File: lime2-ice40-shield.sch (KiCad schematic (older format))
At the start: 5 parts

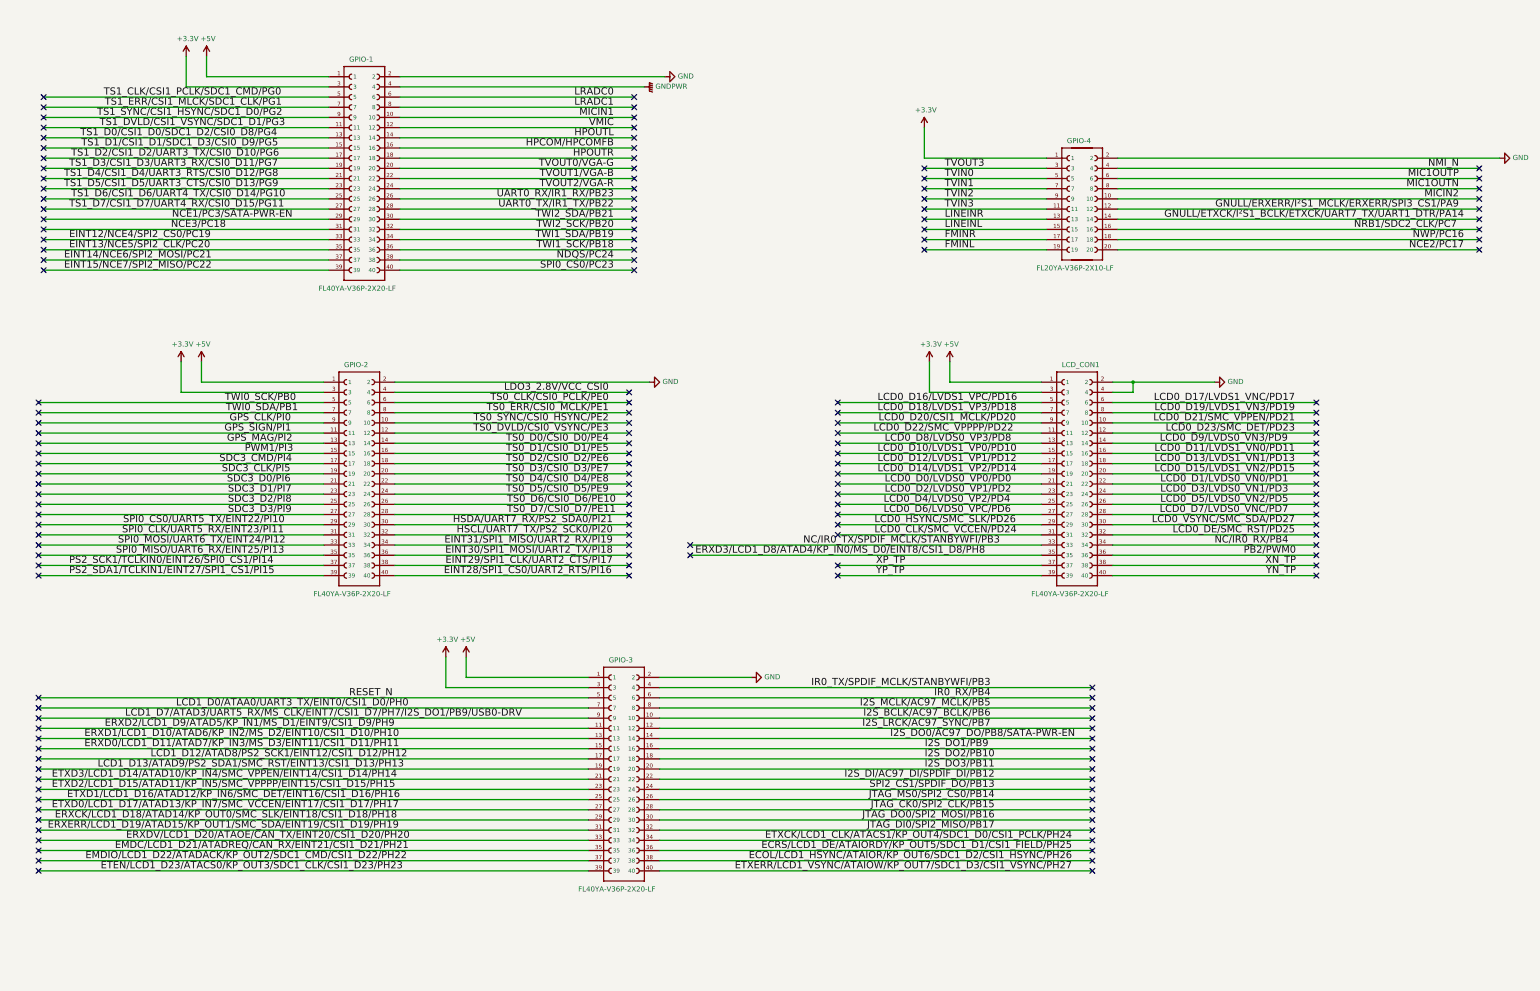
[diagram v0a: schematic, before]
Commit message: Clean up lime2 header connections
Left only those that will be used

Signed-off-by: Rangel Ivanov <rangelivanov88@gmail.com>
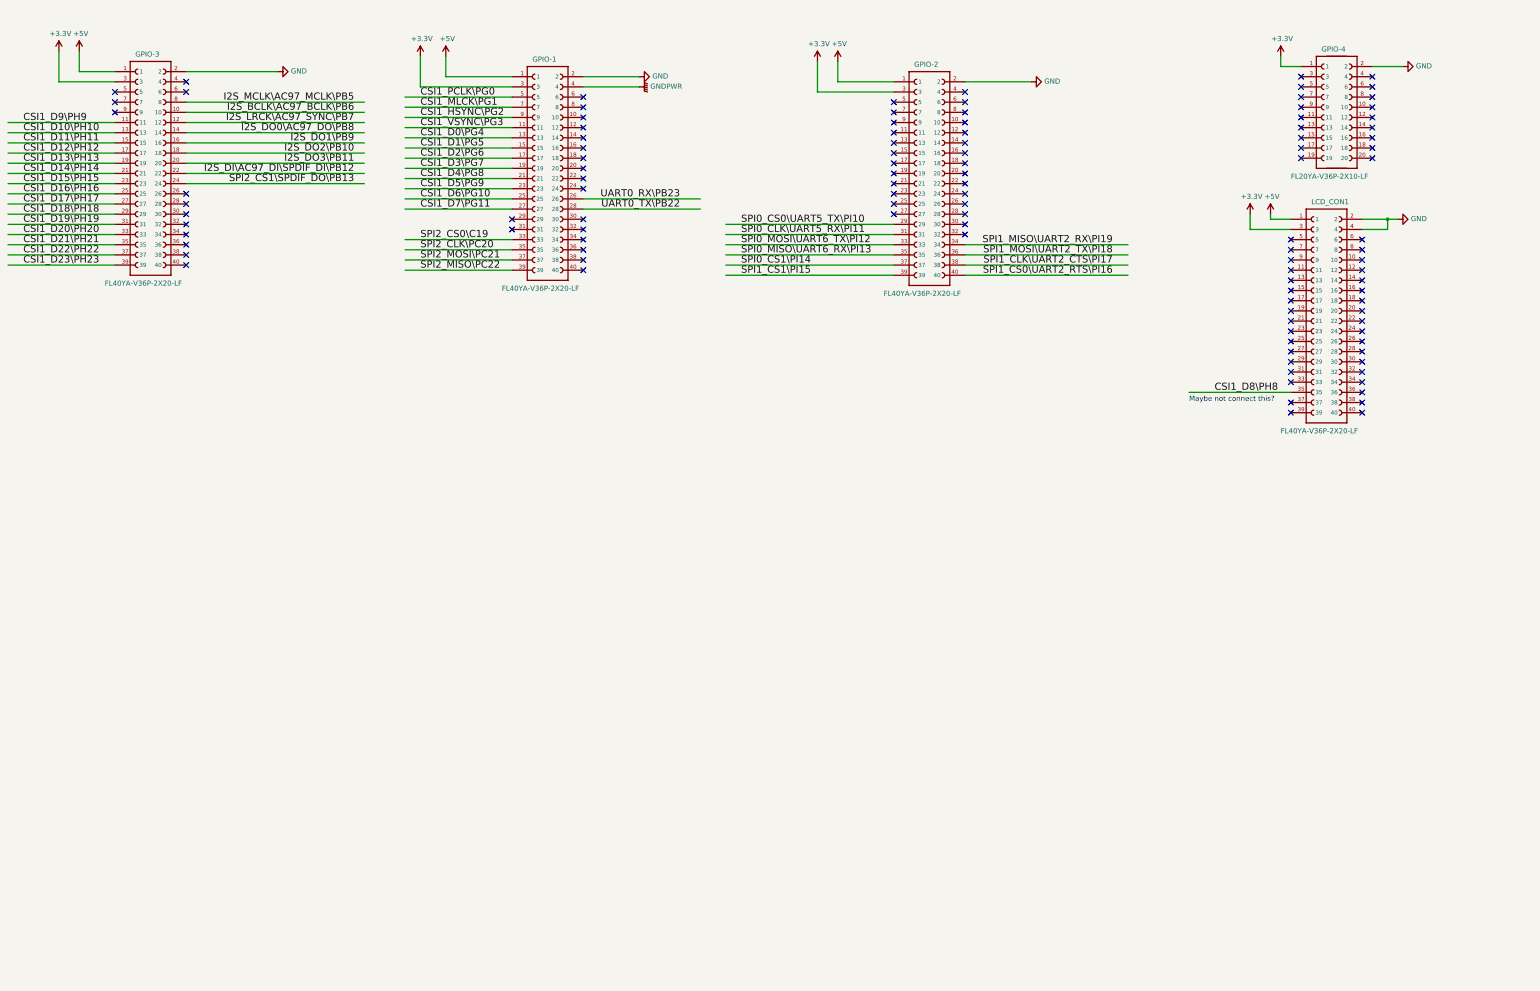
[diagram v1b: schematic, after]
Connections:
- net labels added: CSI1_D0\PG4, CSI1_D10\PH10, CSI1_D11\PH11, CSI1_D12\PH12, CSI1_D13\PH13, CSI1_D14\PH14, CSI1_D15\PH15, CSI1_D16\PH16, CSI1_D17\PH17, CSI1_D18\PH18, CSI1_D19\PH19, CSI1_D1\PG5, CSI1_D20\PH20, CSI1_D21\PH21, CSI1_D22\PH22, CSI1_D23\PH23, CSI1_D2\PG6, CSI1_D3\PG7, CSI1_D4\PG8, CSI1_D5\PG9, CSI1_D6\PG10, CSI1_D7\PG11, CSI1_D8\PH8, CSI1_D9\PH9, CSI1_HSYNC\PG2, CSI1_MLCK\PG1, CSI1_PCLK\PG0, CSI1_VSYNC\PG3, I2S_BCLK\AC97_BCLK\PB6, I2S_DI\AC97_DI\SPDIF_DI\PB12, I2S_DO0\AC97_DO\PB8, I2S_DO1\PB9, I2S_DO2\PB10, I2S_DO3\PB11, I2S_LRCK\AC97_SYNC\PB7, I2S_MCLK\AC97_MCLK\PB5, SPI0_CLK\UART5_RX\PI11, SPI0_CS0\UART5_TX\PI10, SPI0_CS1\PI14, SPI0_MISO\UART6_RX\PI13, SPI0_MOSI\UART6_TX\PI12, SPI1_CLK\UART2_CTS\PI17, SPI1_CS0\UART2_RTS\PI16, SPI1_CS1\PI15, SPI1_MISO\UART2_RX\PI19, SPI1_MOSI\UART2_TX\PI18, SPI2_CLK\PC20, SPI2_CS0\C19, SPI2_CS1\SPDIF_DO\PB13, SPI2_MISO\PC22, SPI2_MOSI\PC21, UART0_RX\PB23, UART0_TX\PB22
- net labels removed: ECOL/LCD1_HSYNC/ATAIOR/KP_OUT6/SDC1_D2/CSI1_HSYNC/PH26, ECRS/LCD1_DE/ATAIORDY/KP_OUT5/SDC1_D1/CSI1_FIELD/PH25, EINT12/NCE4/SPI2_CS0/PC19, EINT13/NCE5/SPI2_CLK/PC20, EINT14/NCE6/SPI2_MOSI/PC21, EINT15/NCE7/SPI2_MISO/PC22, EINT28/SPI1_CS0/UART2_RTS/PI16, EINT29/SPI1_CLK/UART2_CTS/PI17, EINT30/SPI1_MOSI/UART2_TX/PI18, EINT31/SPI1_MISO/UART2_RX/PI19, EMDC/LCD1_D21/ATADREQ/CAN_RX/EINT21/CSI1_D21/PH21, EMDIO/LCD1_D22/ATADACK/KP_OUT2/SDC1_CMD/CSI1_D22/PH22, ERXCK/LCD1_D18/ATAD14/KP_OUT0/SMC_SLK/EINT18/CSI1_D18/PH18, ERXD0/LCD1_D11/ATAD7/KP_IN3/MS_D3/EINT11/CSI1_D11/PH11, ERXD1/LCD1_D10/ATAD6/KP_IN2/MS_D2/EINT10/CSI1_D10/PH10, ERXD2/LCD1_D9/ATAD5/KP_IN1/MS_D1/EINT9/CSI1_D9/PH9, ERXD3/LCD1_D8/ATAD4/KP_IN0/MS_D0/EINT8/CSI1_D8/PH8, ERXDV/LCD1_D20/ATAOE/CAN_TX/EINT20/CSI1_D20/PH20, ERXERR/LCD1_D19/ATAD15/KP_OUT1/SMC_SDA/EINT19/CSI1_D19/PH19, ETEN/LCD1_D23/ATACS0/KP_OUT3/SDC1_CLK/CSI1_D23/PH23, ETXCK/LCD1_CLK/ATACS1/KP_OUT4/SDC1_D0/CSI1_PCLK/PH24, ETXD0/LCD1_D17/ATAD13/KP_IN7/SMC_VCCEN/EINT17/CSI1_D17/PH17, ETXD1/LCD1_D16/ATAD12/KP_IN6/SMC_DET/EINT16/CSI1_D16/PH16, ETXD2/LCD1_D15/ATAD11/KP_IN5/SMC_VPPPP/EINT15/CSI1_D15/PH15, ETXD3/LCD1_D14/ATAD10/KP_IN4/SMC_VPPEN/EINT14/CSI1_D14/PH14, ETXERR/LCD1_VSYNC/ATAIOW/KP_OUT7/SDC1_D3/CSI1_VSYNC/PH27, FMINL, FMINR, GNULL/ERXERR/I²S1_MCLK/ERXERR/SPI3_CS1/PA9, GNULL/ETXCK/I²S1_BCLK/ETXCK/UART7_TX/UART1_DTR/PA14, GPS_CLK/PI0, GPS_MAG/PI2, GPS_SIGN/PI1, HPCOM/HPCOMFB, HPOUTL, HPOUTR, HSCL/UART7_TX/PS2_SCK0/PI20, HSDA/UART7_RX/PS2_SDA0/PI21, I2S_BCLK/AC97_BCLK/PB6, I2S_DI/AC97_DI/SPDIF_DI/PB12, I2S_DO0/AC97_DO/PB8/SATA-PWR-EN, I2S_DO1/PB9, I2S_DO2/PB10, I2S_DO3/PB11, I2S_LRCK/AC97_SYNC/PB7, I2S_MCLK/AC97_MCLK/PB5, IR0_RX/PB4, IR0_TX/SPDIF_MCLK/STANBYWFI/PB3, JTAG_CK0/SPI2_CLK/PB15, JTAG_DI0/SPI2_MISO/PB17, JTAG_DO0/SPI2_MOSI/PB16, JTAG_MS0/SPI2_CS0/PB14, LCD0_CLK/SMC_VCCEN/PD24, LCD0_D0/LVDS0_VP0/PD0, LCD0_D1/LVDS0_VN0/PD1, LCD0_D10/LVDS1_VP0/PD10, LCD0_D11/LVDS1_VN0/PD11, LCD0_D12/LVDS1_VP1/PD12, LCD0_D13/LVDS1_VN1/PD13, LCD0_D14/LVDS1_VP2/PD14, LCD0_D15/LVDS1_VN2/PD15, LCD0_D16/LVDS1_VPC/PD16, LCD0_D17/LVDS1_VNC/PD17, LCD0_D18/LVDS1_VP3/PD18, LCD0_D19/LVDS1_VN3/PD19, LCD0_D2/LVDS0_VP1/PD2, LCD0_D20/CSI1_MCLK/PD20, LCD0_D21/SMC_VPPEN/PD21, LCD0_D22/SMC_VPPPP/PD22, LCD0_D23/SMC_DET/PD23, LCD0_D3/LVDS0_VN1/PD3, LCD0_D4/LVDS0_VP2/PD4, LCD0_D5/LVDS0_VN2/PD5, LCD0_D6/LVDS0_VPC/PD6, LCD0_D7/LVDS0_VNC/PD7, LCD0_D8/LVDS0_VP3/PD8, LCD0_D9/LVDS0_VN3/PD9, LCD0_DE/SMC_RST/PD25, LCD0_HSYNC/SMC_SLK/PD26, LCD0_VSYNC/SMC_SDA/PD27, LCD1_D0/ATAA0/UART3_TX/EINT0/CSI1_D0/PH0, LCD1_D12/ATAD8/PS2_SCK1/EINT12/CSI1_D12/PH12, LCD1_D13/ATAD9/PS2_SDA1/SMC_RST/EINT13/CSI1_D13/PH13, LCD1_D7/ATAD3/UART5_RX/MS_CLK/EINT7/CSI1_D7/PH7/I2S_DO1/PB9/USB0-DRV, LDO3_2.8V/VCC_CSI0, LINEINL, LINEINR, LRADC0, LRADC1, MIC1OUTN, MIC1OUTP, MICIN1, MICIN2, NC/IR0_RX/PB4, NC/IR0_TX/SPDIF_MCLK/STANBYWFI/PB3, NCE1/PC3/SATA-PWR-EN, NCE2/PC17, NCE3/PC18, NDQS/PC24, NMI_N, NRB1/SDC2_CLK/PC7, NWP/PC16, PB2/PWM0, PS2_SCK1/TCLKIN0/EINT26/SPI0_CS1/PI14, PS2_SDA1/TCLKIN1/EINT27/SPI1_CS1/PI15, PWM1/PI3, RESET_N, SDC3_CLK/PI5, SDC3_CMD/PI4, SDC3_D0/PI6, SDC3_D1/PI7, SDC3_D2/PI8, SDC3_D3/PI9, SPI0_CLK/UART5_RX/EINT23/PI11, SPI0_CS0/PC23, SPI0_CS0/UART5_TX/EINT22/PI10, SPI0_MISO/UART6_RX/EINT25/PI13, SPI0_MOSI/UART6_TX/EINT24/PI12, SPI2_CS1/SPDIF_DO/PB13, TS0_CLK/CSI0_PCLK/PE0, TS0_D0/CSI0_D0/PE4, TS0_D1/CSI0_D1/PE5, TS0_D2/CSI0_D2/PE6, TS0_D3/CSI0_D3/PE7, TS0_D4/CSI0_D4/PE8, TS0_D5/CSI0_D5/PE9, TS0_D6/CSI0_D6/PE10, TS0_D7/CSI0_D7/PE11, TS0_DVLD/CSI0_VSYNC/PE3, TS0_ERR/CSI0_MCLK/PE1, TS0_SYNC/CSI0_HSYNC/PE2, TS1_CLK/CSI1_PCLK/SDC1_CMD/PG0, TS1_D0/CSI1_D0/SDC1_D2/CSI0_D8/PG4, TS1_D1/CSI1_D1/SDC1_D3/CSI0_D9/PG5, TS1_D2/CSI1_D2/UART3_TX/CSI0_D10/PG6, TS1_D3/CSI1_D3/UART3_RX/CSI0_D11/PG7, TS1_D4/CSI1_D4/UART3_RTS/CSI0_D12/PG8, TS1_D5/CSI1_D5/UART3_CTS/CSI0_D13/PG9, TS1_D6/CSI1_D6/UART4_TX/CSI0_D14/PG10, TS1_D7/CSI1_D7/UART4_RX/CSI0_D15/PG11, TS1_DVLD/CSI1_VSYNC/SDC1_D1/PG3, TS1_ERR/CSI1_MLCK/SDC1_CLK/PG1, TS1_SYNC/CSI1_HSYNC/SDC1_D0/PG2, TVIN0, TVIN1, TVIN2, TVIN3, TVOUT0/VGA-G, TVOUT1/VGA-B, TVOUT2/VGA-R, TVOUT3, TWI0_SCK/PB0, TWI0_SDA/PB1, TWI1_SCK/PB18, TWI1_SDA/PB19, TWI2_SCK/PB20, TWI2_SDA/PB21, UART0_RX/IR1_RX/PB23, UART0_TX/IR1_TX/PB22, VMIC, XN_TP, XP_TP, YN_TP, YP_TP
- wire segments 191 -> 80
- no-connect marks 164 -> 111
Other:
- note added: "Maybe not connect this?\n"
- moved on the sheet: GPIO-1, GPIO-2, GPIO-3, GPIO-4, LCD_CON1

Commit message: Initial routing of CSI1 signals
Signed-off-by: Rangel Ivanov <rangelivanov88@gmail.com>
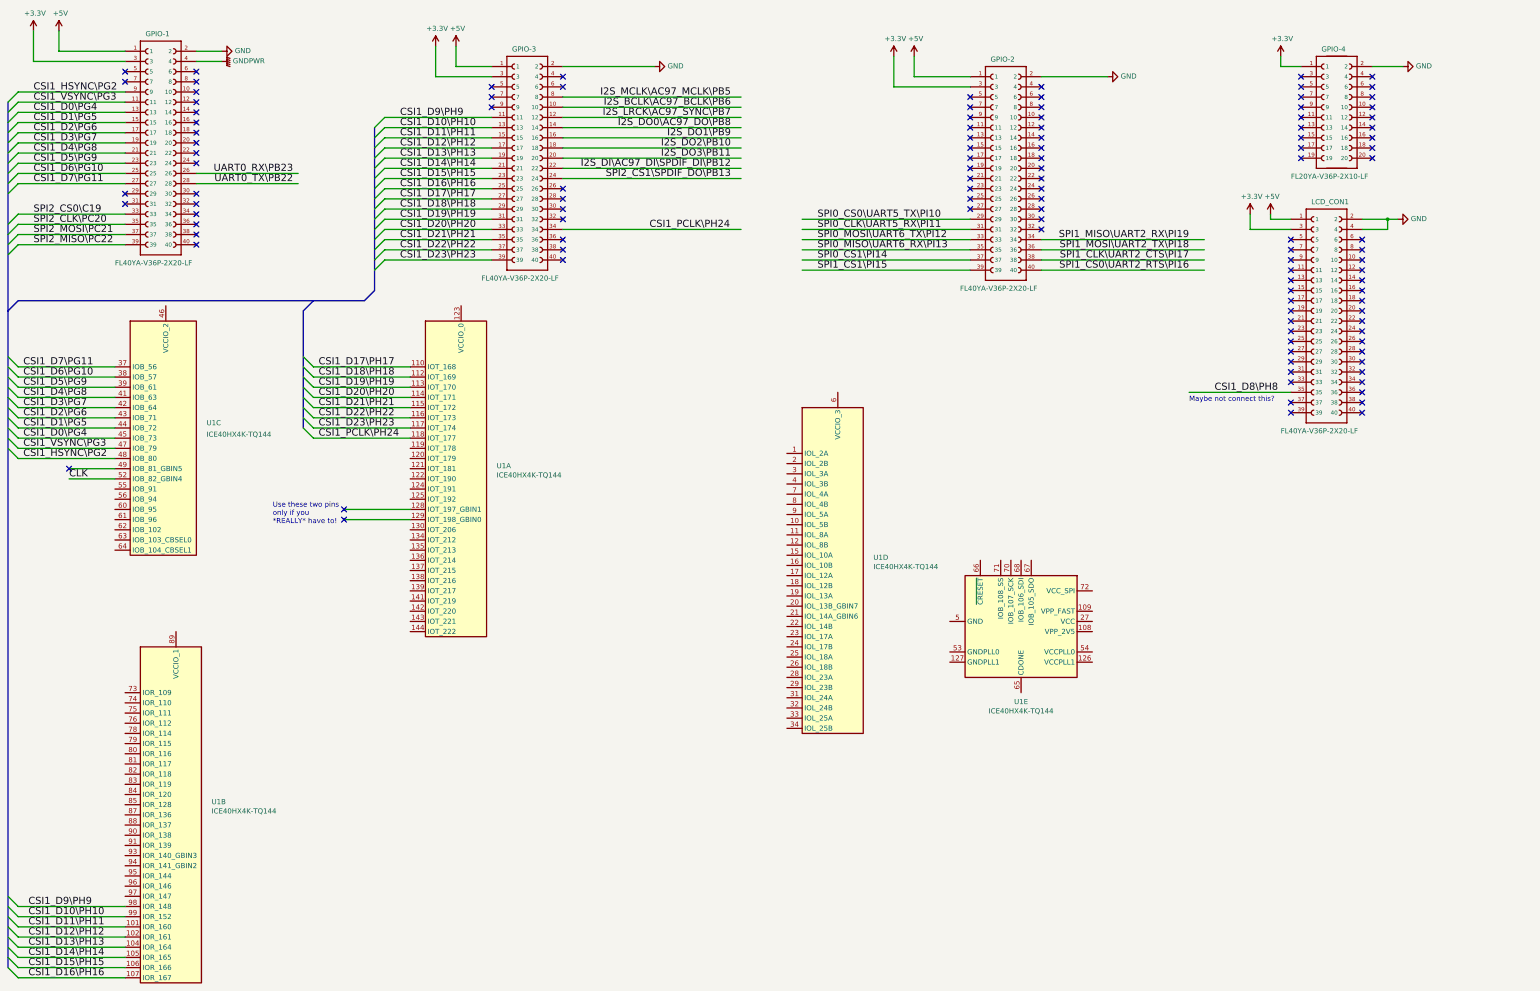
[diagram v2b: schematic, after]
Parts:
- added U1: ICE40HX4K-TQ144, lime2-ice40-shield:TQFP-144_20x20mm_P0.5mm, symbol lime2-ice40-shield:ICE40HX4K-TQ144
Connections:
- net labels added: CLK, CSI1_PCLK\PH24
- net labels removed: CSI1_MLCK\PG1, CSI1_PCLK\PG0
- wire segments 80 -> 109
- no-connect marks 111 -> 115
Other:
- note added: "Use these two pins \nonly if you\n*REALLY* have to!\n"
- moved on the sheet: GPIO-1, GPIO-2, GPIO-3

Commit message: Initial routing of SDRAM
Signed-off-by: Rangel Ivanov <rangelivanov88@gmail.com>
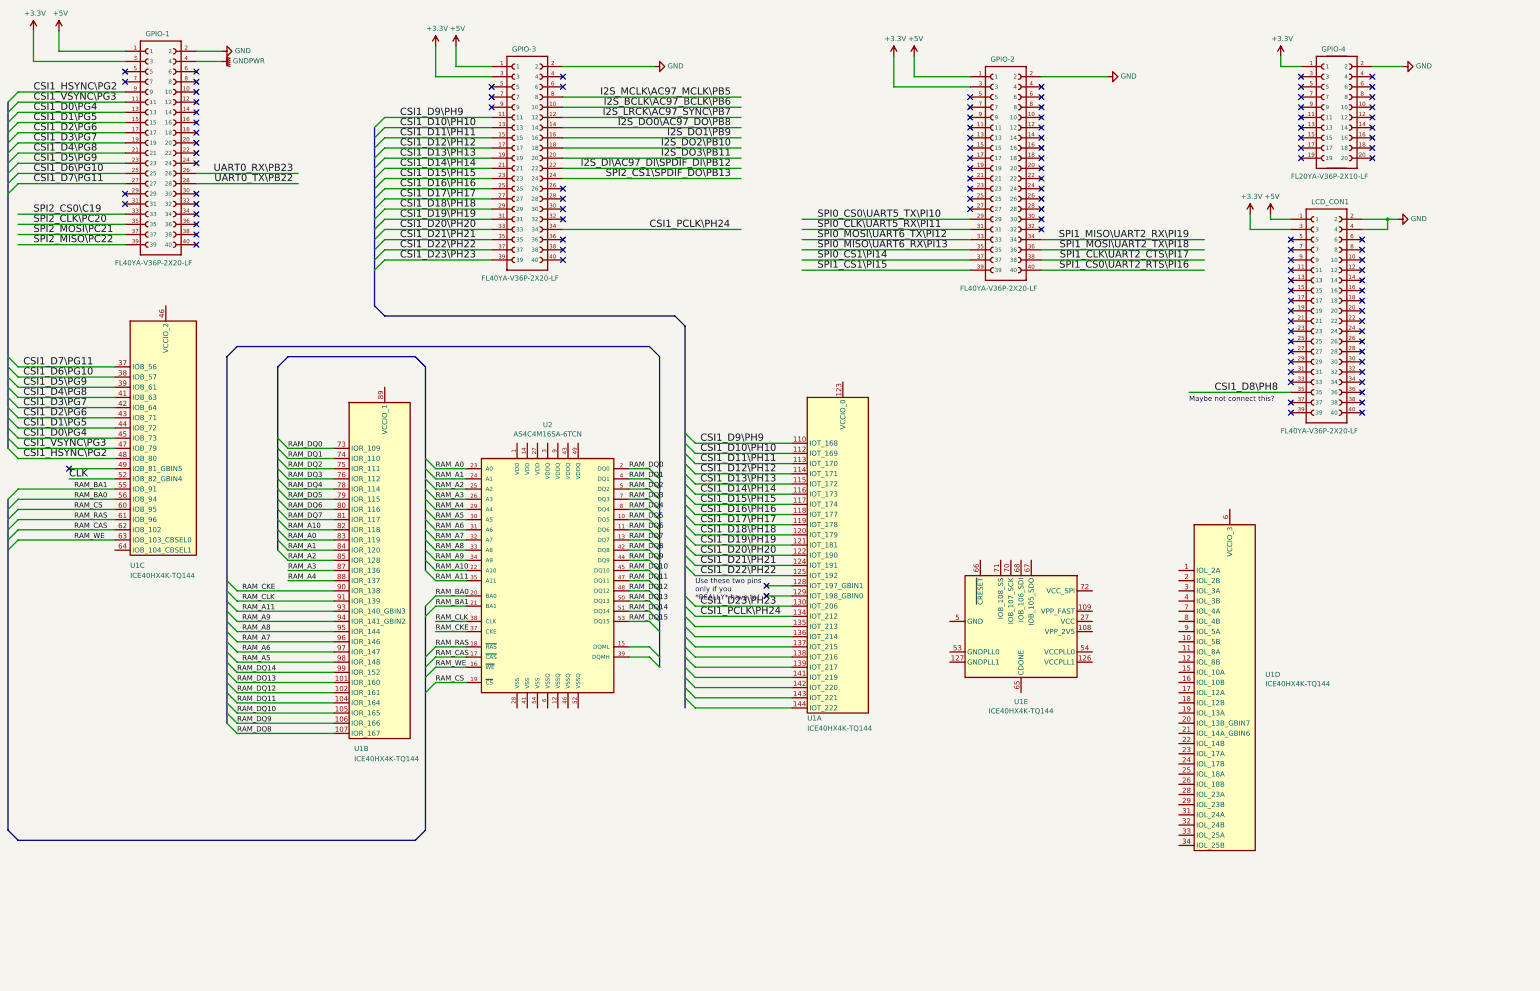
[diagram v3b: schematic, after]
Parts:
- added U2: AS4C4M16SA-6TCN, lime2-ice40-shield:TSOP-II-54_22.2x10.16mm_P0.8mm, symbol Memory_RAM:AS4C4M16SA
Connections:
- net labels added: RAM_A0, RAM_A1, RAM_A10, RAM_A11, RAM_A2, RAM_A3, RAM_A4, RAM_A5, RAM_A6, RAM_A7, RAM_A8, RAM_A9, RAM_BA0, RAM_BA1, RAM_CAS, RAM_CKE, RAM_CLK, RAM_CS, RAM_DQ0, RAM_DQ1, RAM_DQ10, RAM_DQ11, RAM_DQ12, RAM_DQ13, RAM_DQ14, RAM_DQ15, RAM_DQ2, RAM_DQ3, RAM_DQ4, RAM_DQ5, RAM_DQ6, RAM_DQ7, RAM_DQ8, RAM_DQ9, RAM_RAS, RAM_WE
- wire segments 109 -> 191
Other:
- moved on the sheet: U1A, U1B, U1D
